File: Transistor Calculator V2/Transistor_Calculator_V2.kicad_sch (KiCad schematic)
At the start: 61 parts, among them J1 5V, J2 GND, Q1 2N3904, Q10 2N3904, Q11 2N3904, Q12 2N3904, Q13 2N3904, Q14 2N3904, Q15 2N3904, Q16 2N3904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

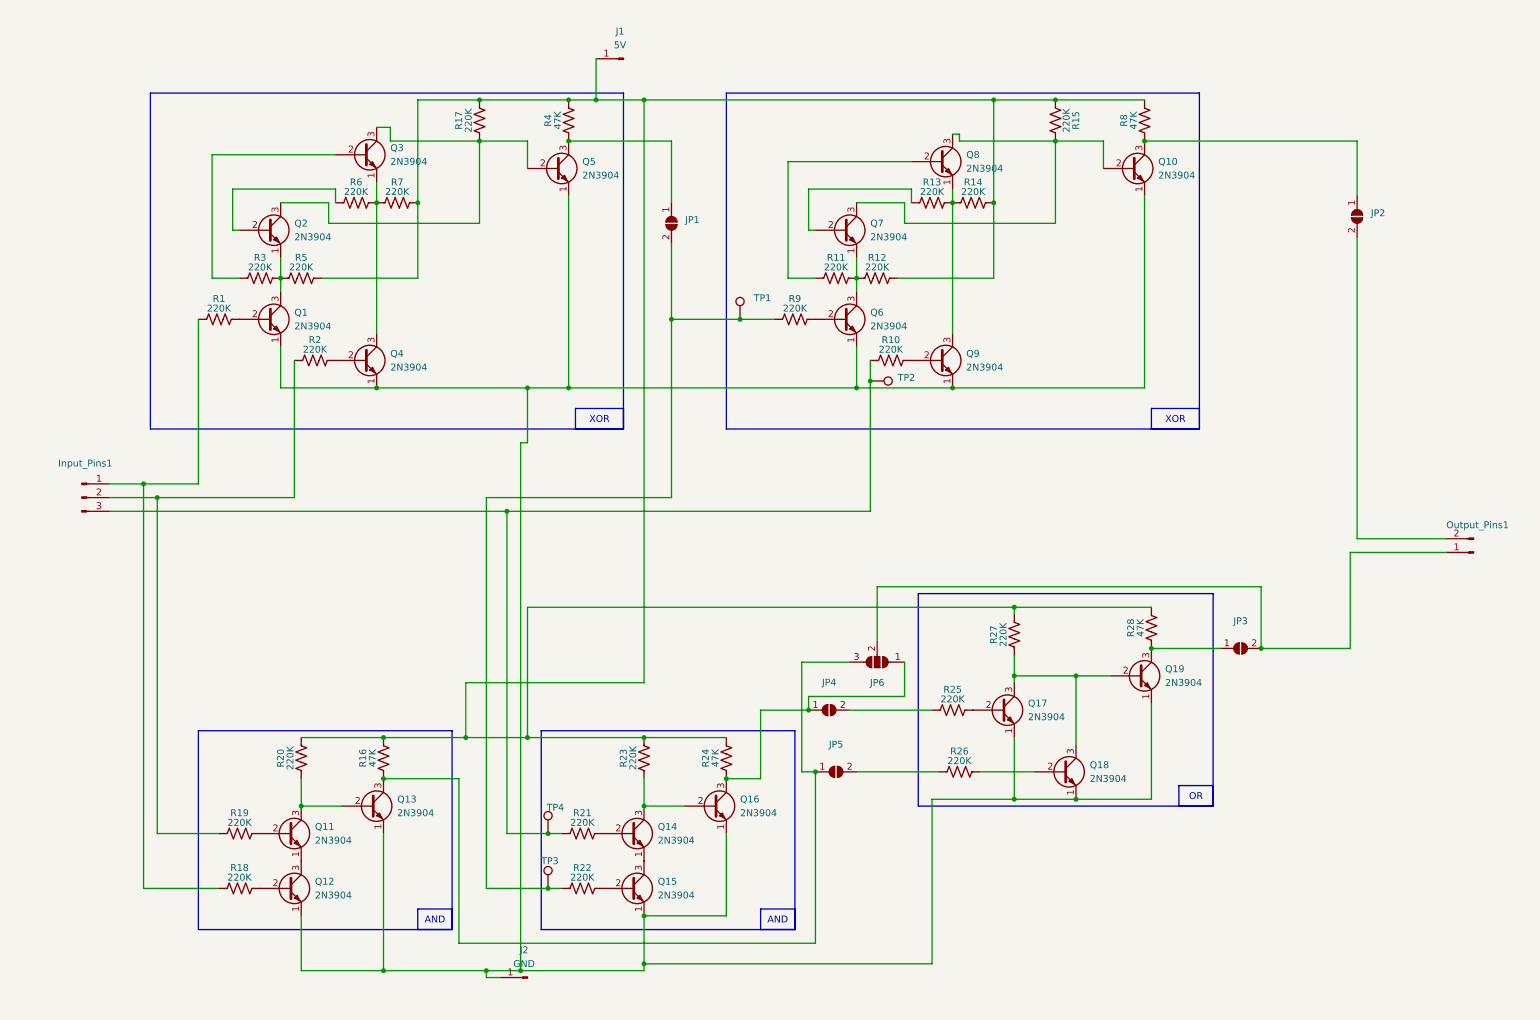
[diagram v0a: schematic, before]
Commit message: Changes some routing. Added LED for debugging.
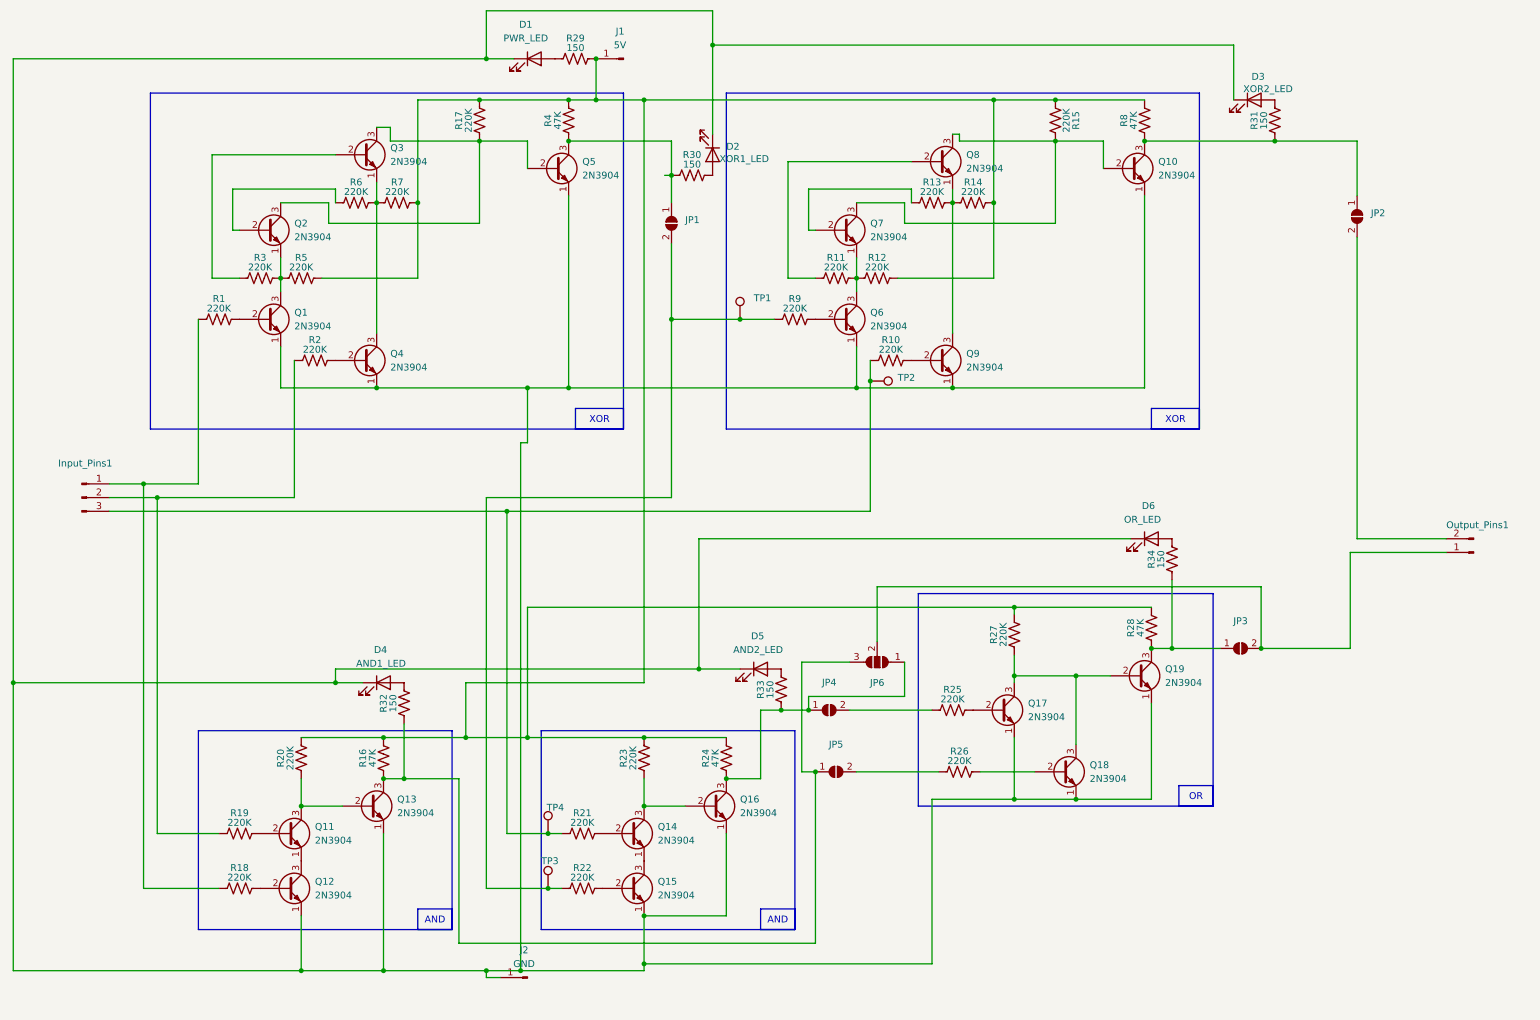
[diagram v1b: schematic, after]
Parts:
- added D1: PWR_LED, LED_THT:LED_D5.0mm, symbol Device:LED
- added D2: XOR1_LED, LED_THT:LED_D5.0mm, symbol Device:LED
- added D3: XOR2_LED, LED_THT:LED_D5.0mm, symbol Device:LED
- added D4: AND1_LED, LED_THT:LED_D5.0mm, symbol Device:LED
- added D5: AND2_LED, LED_THT:LED_D5.0mm, symbol Device:LED
- added D6: OR_LED, LED_THT:LED_D5.0mm, symbol Device:LED
- added R29, R30, R31, R32, R33, R34: 150, Resistor_THT:R_Axial_DIN0207_L6.3mm_D2.5mm_P2.54mm_Vertical, symbol Device:R_US
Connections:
- net at J2.1 (Pin_1), Q1.1 (E), Q10.1 (E)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: now also D1.1 (K), D2.1 (K), D3.1 (K), D4.1 (K), D5.1 (K), D6.1 (K)
- net at JP3.1 (A), Q19.3 (C), R28.1: now also R34.1
- net at JP4.1 (A), JP6.1 (A), Q16.3 (C)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: now also R33.1
- net at J1.1 (Pin_1), R12.2, R14.2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: now also R29.2
- net at JP5.1 (A), JP6.3 (B), Q13.3 (C)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: now also R32.1
- net at JP2.1 (A), Q10.3 (C), R8.1: now also R31.1
- net at JP1.1 (A), Q5.3 (C), R4.1: now also R30.1
- new net: D5.2 (A), R33.2
- new net: D1.2 (A), R29.1
- new net: D4.2 (A), R32.2
- new net: D6.2 (A), R34.2
- new net: D3.2 (A), R31.2
- new net: D2.2 (A), R30.2

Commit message: Small changes
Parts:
- added J3: 5V_Out, Connector_Pin:Pin_D1.0mm_L10.0mm_LooseFit, symbol Connector:Conn_01x01_Pin
- added J4: GND_Out, Connector_Pin:Pin_D1.0mm_L10.0mm_LooseFit, symbol Connector:Conn_01x01_Pin
- J1: value 5V -> 5V_In
- J2: value GND -> GND_In
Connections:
- net at D1.1 (K), D2.1 (K), D3.1 (K)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: now also J4.1 (Pin_1)
- net at J1.1 (Pin_1), R12.2, R14.2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: now also J3.1 (Pin_1)
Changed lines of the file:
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@@
 	)
 	(junction
+		(at 124.46 31.75)
+		(diameter 0)
+		(color 0 0 0 0)
+	)
+	(junction
 		(at 127 72.39)
 		(diameter 0)
@@
 	)
 	(junction
+		(at 114.3 193.04)
+		(diameter 0)
+		(color 0 0 0 0)
+	)
+	(junction
 		(at 104.14 177.8)
 		(diameter 0)
@@
 	(wire
 		(pts
+			(xy 114.3 193.04) (xy 121.92 193.04)
+		)
+		(stroke
+			(width 0)
+			(type default)
+		)
+	)
+	(wire
+		(pts
 			(xy 121.92 139.7) (xy 121.92 31.75)
 		)
@@
 	(wire
 		(pts
-			(xy 121.92 31.75) (xy 186.69 31.75)
+			(xy 121.92 31.75) (xy 124.46 31.75)
 		)
 		(stroke
@@
 	(wire
 		(pts
-			(xy 99.06 193.04) (xy 121.92 193.04)
+			(xy 99.06 193.04) (xy 114.3 193.04)
 		)
 		(stroke
@@
 	(wire
 		(pts
+			(xy 124.46 31.75) (xy 186.69 31.75)
+		)
+		(stroke
+			(width 0)
+			(type default)
+		)
+	)
+	(wire
+		(pts
 			(xy 73.66 167.64) (xy 73.66 193.04)
 		)
@@
 	(symbol
 		(lib_id "Connector:Conn_01x01_Pin")
+		(at 124.46 26.67 270)
+		(unit 1)
+		(exclude_from_sim no)
+		(in_bom yes)
+		(on_board yes)
+		(dnp no)
+		(fields_autoplaced yes)
+		(property "Reference" "J3"
+			(at 125.73 26.0349 90)
+			(effects
+				(font
+					(size 1.27 1.27)
+				)
+				(justify left)
+			)
+		)
+		(property "Value" "5V_Out"
+			(at 125.73 28.5749 90)
+			(effects
+				(font
+					(size 1.27 1.27)
+				)
+				(justify left)
+			)
+		)
+		(property "Footprint" "Connector_Pin:Pin_D1.0mm_L10.0mm_LooseFit"
+			(at 124.46 26.67 0)
+			(effects
+				(font
+					(size 1.27 1.27)
+				)
+				(hide yes)
+			)
+		)
+		(property "Datasheet" "~"
+			(at 124.46 26.67 0)
+			(effects
+				(font
+					(size 1.27 1.27)
+				)
+				(hide yes)
+			)
+		)
+		(property "Description" "Generic connector, single row, 01x01, script generated"
+			(at 124.46 26.67 0)
+			(effects
+				(font
+					(size 1.27 1.27)
+				)
+				(hide yes)
+			)
+		)
+		(pin "1"
+		)
+		(instances
+			(project "Transistor_Calculator_V2"
+				(path "/4e74c2aa-3410-4407-95d8-73d62854742b"
+					(reference "J3")
+					(unit 1)
+				)
+			)
+		)
+	)
+	(symbol
+		(lib_id "Connector:Conn_01x01_Pin")
 		(at 118.11 24.13 180)
 		(unit 1)
@@
 			)
 		)
-		(property "Value" "5V"
+		(property "Value" "5V_In"
 			(at 117.475 21.59 0)
 			(effects
@@
 	)
 	(symbol
+		(lib_id "Connector:Conn_01x01_Pin")
+		(at 114.3 198.12 90)
+		(unit 1)
+		(exclude_from_sim no)
+		(in_bom yes)
+		(on_board yes)
+		(dnp no)
+		(fields_autoplaced yes)
+		(property "Reference" "J4"
+			(at 115.57 196.2149 90)
+			(effects
+				(font
+					(size 1.27 1.27)
+				)
+				(justify right)
+			)
+		)
+		(property "Value" "GND_Out"
+			(at 115.57 198.7549 90)
+			(effects
+				(font
+					(size 1.27 1.27)
+				)
+				(justify right)
+			)
+		)
+		(property "Footprint" "Connector_Pin:Pin_D1.0mm_L10.0mm_LooseFit"
+			(at 114.3 198.12 0)
+			(effects
+				(font
+					(size 1.27 1.27)
+				)
+				(hide yes)
+			)
+		)
+		(property "Datasheet" "~"
+			(at 114.3 198.12 0)
+			(effects
+				(font
+					(size 1.27 1.27)
+				)
+				(hide yes)
+			)
+		)
+		(property "Description" "Generic connector, single row, 01x01, script generated"
+			(at 114.3 198.12 0)
+			(effects
+				(font
+					(size 1.27 1.27)
+				)
+				(hide yes)
+			)
+		)
+		(pin "1"
+		)
+		(instances
+			(project "Transistor_Calculator_V2"
+				(path "/4e74c2aa-3410-4407-95d8-73d62854742b"
+					(reference "J4")
+					(unit 1)
+				)
+			)
+		)
+	)
+	(symbol
 		(lib_id "Transistor_BJT:2N3904")
 		(at 55.88 167.64 0)
@@
 			)
 		)
-		(property "Value" "GND"
+		(property "Value" "GND_In"
 			(at 99.695 191.77 0)
 			(effects

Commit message: removed LED
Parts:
- removed D2: XOR1_LED, LED_THT:LED_D5.0mm, symbol Device:LED
- removed D3: XOR2_LED, LED_THT:LED_D5.0mm, symbol Device:LED
- removed D4: AND1_LED, LED_THT:LED_D5.0mm, symbol Device:LED
- removed D5: AND2_LED, LED_THT:LED_D5.0mm, symbol Device:LED
- removed D6: OR_LED, LED_THT:LED_D5.0mm, symbol Device:LED
- removed R30, R31, R32, R33, R34: 150, Resistor_THT:R_Axial_DIN0207_L6.3mm_D2.5mm_P2.54mm_Vertical, symbol Device:R_US

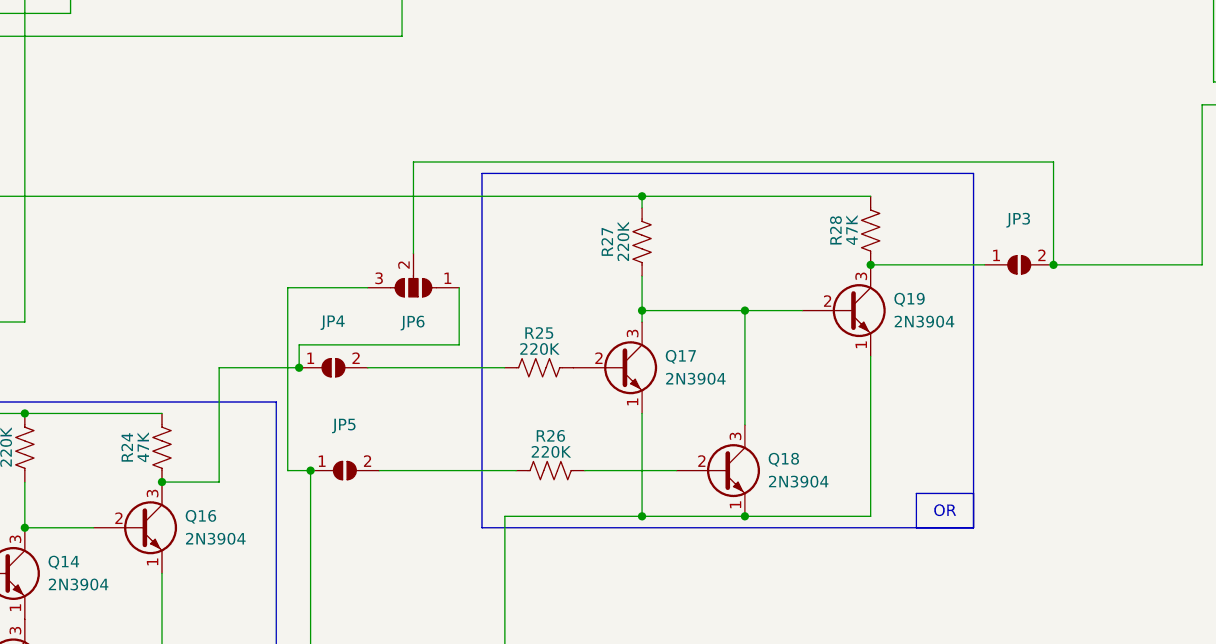
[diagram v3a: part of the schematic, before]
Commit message: Added diode and changes some of the pcb placements
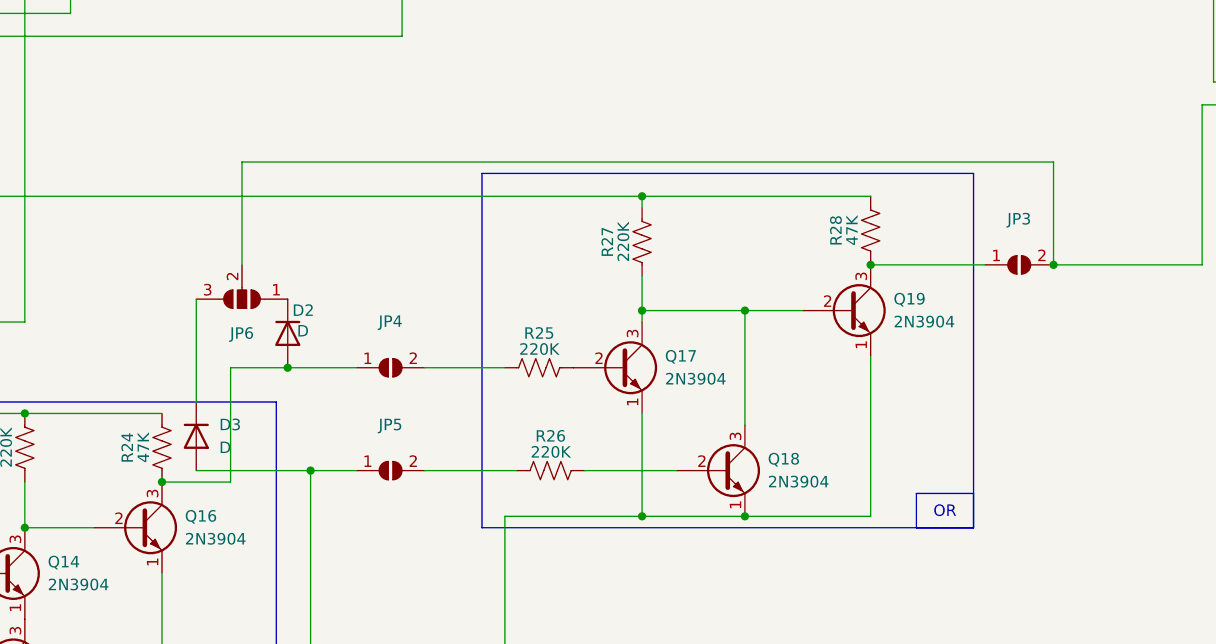
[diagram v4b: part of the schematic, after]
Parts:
- added D2, D3: D, Diode_THT:D_A-405_P2.54mm_Vertical_AnodeUp, symbol Device:D
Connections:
- net at JP4.1 (A), Q16.3 (C), R24.1: now also D2.2 (A); no longer JP6.1 (A)
- net at JP5.1 (A), Q13.3 (C), R16.1: now also D3.2 (A); no longer JP6.3 (B)
- new net: D2.1 (K), JP6.1 (A)
- new net: D3.1 (K), JP6.3 (B)
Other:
- moved on the sheet: JP4, JP5, JP6
